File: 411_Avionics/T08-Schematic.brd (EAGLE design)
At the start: 63.1 x 25.4 mm, 42 parts, among them IC1 BQ24022, J1 USB-MICROB, J3 JST-PH-2-SMT-RA, U1 LP5907, U2 M25P10-AVMN6TP_TR, U3 LSM9DS0, U5 LTC1998, U6 ATMEGA32U4-AU, X1 8MHz

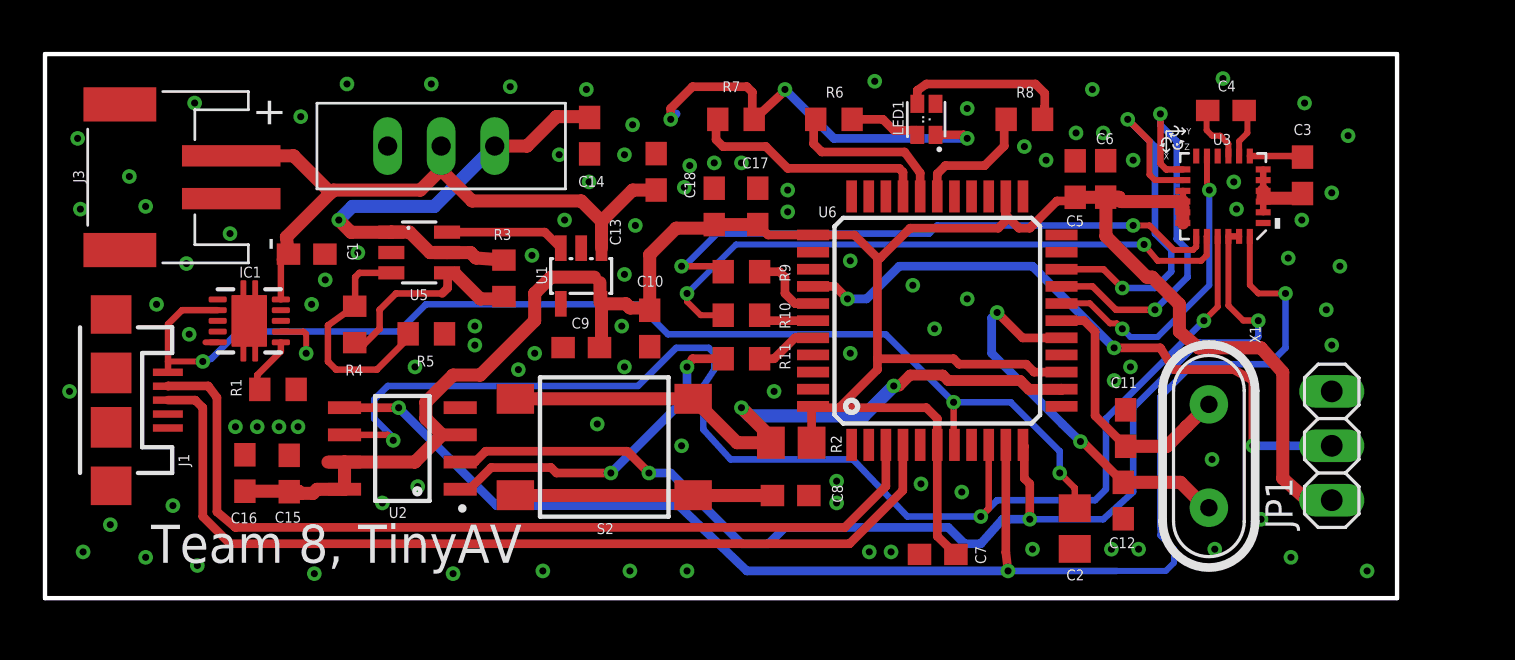
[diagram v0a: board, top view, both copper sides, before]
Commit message: Updated current limiting resistors to 0805 package.  Also fixed some oopsies on the layout (extra traces).
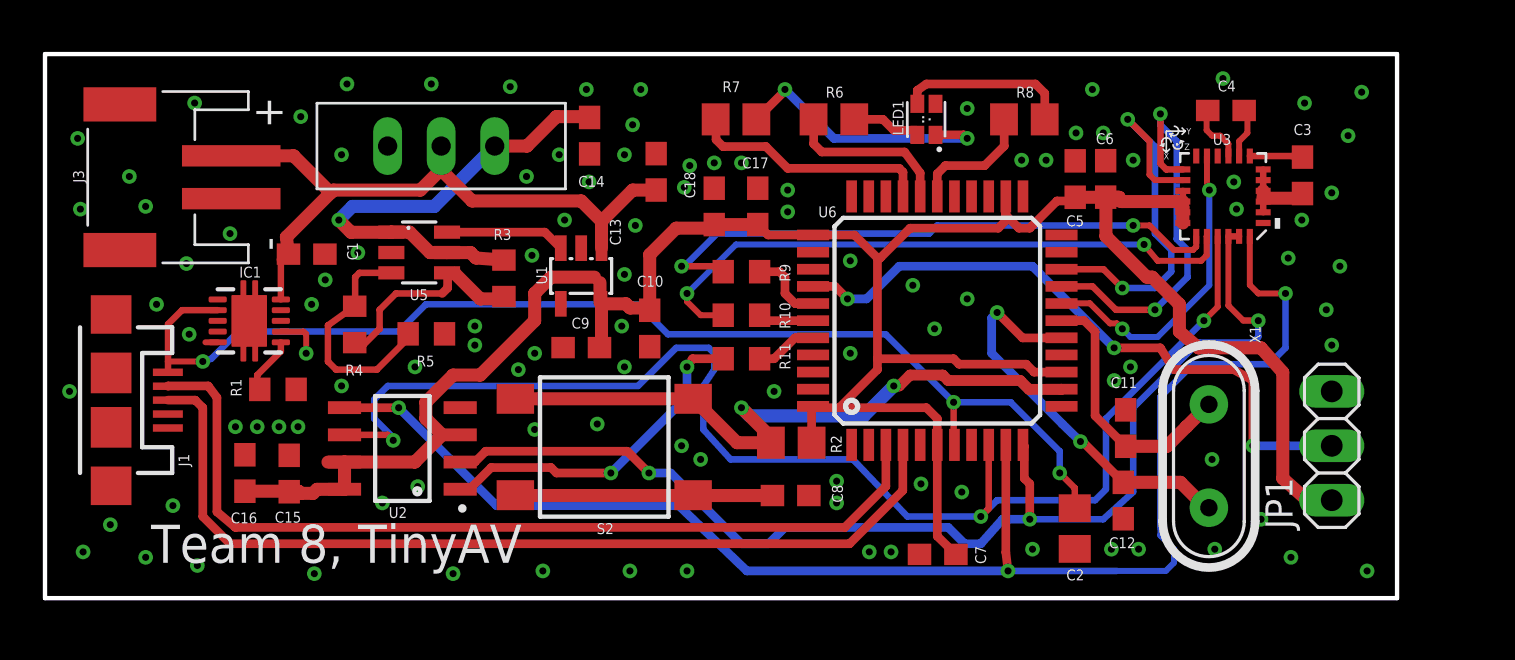
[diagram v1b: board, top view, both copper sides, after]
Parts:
- R6, R7, R8: device rcl:R0603 -> rcl:R0805
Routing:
- net N$1: track 19.5 -> 13.0 mm, vias 3 -> 2
- net GND: vias 99 -> 105
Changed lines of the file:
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@@
 <attribute name="NAME" x="18.183" y="11.322" size="0.508" layer="25" rot="R180"/>
 </element>
-<element name="R6" library="rcl" package="R0603" value="330" x="36.83" y="22.352" smashed="yes">
+<element name="R6" library="rcl" package="R0805" value="330" x="36.83" y="22.352" smashed="yes">
 <attribute name="NAME" x="36.449" y="23.368" size="0.508" layer="25"/>
 </element>
-<element name="R7" library="rcl" package="R0603" value="330" x="32.258" y="22.352" smashed="yes">
+<element name="R7" library="rcl" package="R0805" value="330" x="32.258" y="22.352" smashed="yes">
 <attribute name="NAME" x="31.623" y="23.622" size="0.508" layer="25"/>
 </element>
-<element name="R8" library="rcl" package="R0603" value="330" x="45.72" y="22.352" smashed="yes">
+<element name="R8" library="rcl" package="R0805" value="330" x="45.72" y="22.352" smashed="yes">
 <attribute name="NAME" x="45.339" y="23.368" size="0.508" layer="25"/>
 </element>
@@
 <via x="60.452" y="15.494" extent="1-16" drill="0.3302"/>
 <via x="58.801" y="23.114" extent="1-16" drill="0.3302"/>
-<via x="38.735" y="24.13" extent="1-16" drill="0.3302"/>
 <via x="31.242" y="20.32" extent="1-16" drill="0.3302"/>
 <via x="34.671" y="18.034" extent="1-16" drill="0.3302"/>
-<via x="45.72" y="21.082" extent="1-16" drill="0.3302"/>
+<via x="45.593" y="20.447" extent="1-16" drill="0.3302"/>
 <via x="48.895" y="23.749" extent="1-16" drill="0.3302"/>
 <via x="54.991" y="24.257" extent="1-16" drill="0.3302"/>
@@
 <via x="4.699" y="18.288" extent="1-16" drill="0.3302"/>
 <via x="1.778" y="2.159" extent="1-16" drill="0.3302"/>
+<via x="27.813" y="23.749" extent="1-16" drill="0.3302"/>
+<via x="22.86" y="7.874" extent="1-16" drill="0.3302"/>
+<via x="61.468" y="23.622" extent="1-16" drill="0.3302"/>
+<via x="30.607" y="6.477" extent="1-16" drill="0.3302"/>
+<via x="13.843" y="9.906" extent="1-16" drill="0.3302"/>
+<via x="13.843" y="20.701" extent="1-16" drill="0.3302"/>
+<via x="22.479" y="19.685" extent="1-16" drill="0.3302"/>
 </signal>
 <signal name="N$4">
@@
 <wire x1="40.056" y1="19.888" x2="39.878" y2="20.066" width="0.4064" layer="1"/>
 <wire x1="39.878" y1="20.066" x2="34.671" y2="20.066" width="0.4064" layer="1"/>
-<wire x1="31.242" y1="22.286" x2="31.408" y2="22.352" width="0.4064" layer="1"/>
+<wire x1="31.242" y1="22.286" x2="31.308" y2="22.352" width="0.4064" layer="1"/>
 <wire x1="34.671" y1="20.066" x2="33.655" y2="21.082" width="0.4064" layer="1"/>
 <wire x1="33.655" y1="21.082" x2="31.65" y2="21.082" width="0.4064" layer="1"/>
 <wire x1="31.65" y1="21.082" x2="31.327" y2="21.405" width="0.4064" layer="1"/>
 <wire x1="31.327" y1="21.405" x2="31.327" y2="22.333" width="0.4064" layer="1"/>
-<wire x1="31.327" y1="22.333" x2="31.408" y2="22.352" width="0.4064" layer="1"/>
+<wire x1="31.327" y1="22.333" x2="31.308" y2="22.352" width="0.4064" layer="1"/>
 </signal>
 <signal name="GREEN_LED">
@@
 <wire x1="40.856" y1="19.85" x2="40.132" y2="20.828" width="0.4064" layer="1"/>
 <wire x1="40.132" y1="20.828" x2="36.266" y2="20.828" width="0.4064" layer="1"/>
-<wire x1="35.873" y1="22.345" x2="35.98" y2="22.352" width="0.4064" layer="1"/>
+<wire x1="35.873" y1="22.345" x2="35.88" y2="22.352" width="0.4064" layer="1"/>
 <wire x1="36.266" y1="20.828" x2="35.883" y2="21.211" width="0.4064" layer="1"/>
 <wire x1="35.883" y1="21.211" x2="35.883" y2="22.349" width="0.4064" layer="1"/>
-<wire x1="35.883" y1="22.349" x2="35.98" y2="22.352" width="0.4064" layer="1"/>
+<wire x1="35.883" y1="22.349" x2="35.88" y2="22.352" width="0.4064" layer="1"/>
 </signal>
 <signal name="BLUE_LED">
@@
 <wire x1="43.867" y1="20.193" x2="44.78" y2="21.106" width="0.4064" layer="1"/>
 <wire x1="44.78" y1="21.106" x2="44.78" y2="22.342" width="0.4064" layer="1"/>
-<wire x1="44.78" y1="22.342" x2="44.87" y2="22.352" width="0.4064" layer="1"/>
+<wire x1="44.78" y1="22.342" x2="44.77" y2="22.352" width="0.4064" layer="1"/>
 </signal>
 <signal name="N$1">
 <contactref element="LED1" pad="1"/>
 <contactref element="R7" pad="2"/>
-<wire x1="29.464" y1="22.606" x2="29.21" y2="22.352" width="0.4064" layer="16"/>
-<via x="29.21" y="22.352" extent="1-16" drill="0.3302"/>
-<wire x1="29.21" y1="22.352" x2="29.21" y2="22.86" width="0.4064" layer="1"/>
-<wire x1="29.21" y1="22.86" x2="30.226" y2="23.876" width="0.4064" layer="1"/>
-<wire x1="30.226" y1="23.876" x2="32.766" y2="23.876" width="0.4064" layer="1"/>
-<wire x1="32.766" y1="23.876" x2="33.02" y2="23.622" width="0.4064" layer="1"/>
-<wire x1="33.02" y1="23.622" x2="33.02" y2="22.54" width="0.4064" layer="1"/>
-<wire x1="33.02" y1="22.54" x2="33.108" y2="22.352" width="0.4064" layer="1"/>
 <via x="43.053" y="21.463" extent="1-16" drill="0.3302"/>
 <via x="34.544" y="23.749" extent="1-16" drill="0.3302"/>
 <wire x1="34.544" y1="23.749" x2="34.544" y2="23.688" width="0.4064" layer="1"/>
-<wire x1="34.544" y1="23.688" x2="33.108" y2="22.352" width="0.4064" layer="1"/>
+<wire x1="34.544" y1="23.688" x2="33.208" y2="22.352" width="0.4064" layer="1"/>
 <wire x1="41.573" y1="21.627" x2="42.889" y2="21.627" width="0.4064" layer="1"/>
 <wire x1="42.889" y1="21.627" x2="43.053" y2="21.463" width="0.4064" layer="1"/>
@@
 <contactref element="LED1" pad="2"/>
 <contactref element="R6" pad="2"/>
-<wire x1="37.68" y1="22.352" x2="39.116" y2="22.352" width="0.4064" layer="1"/>
+<wire x1="37.78" y1="22.352" x2="39.116" y2="22.352" width="0.4064" layer="1"/>
 <wire x1="39.116" y1="22.352" x2="39.624" y2="21.844" width="0.4064" layer="1"/>
 <wire x1="39.624" y1="21.844" x2="40.686" y2="21.844" width="0.4064" layer="1"/>
@@
 <contactref element="LED1" pad="3"/>
 <contactref element="R8" pad="2"/>
-<wire x1="46.57" y1="22.352" x2="46.67" y2="22.926" width="0.4064" layer="1"/>
+<wire x1="46.67" y1="22.352" x2="46.67" y2="22.926" width="0.4064" layer="1"/>
 <wire x1="40.723" y1="23.077" x2="40.723" y2="23.705" width="0.4064" layer="1"/>
 <wire x1="40.723" y1="23.705" x2="41.148" y2="24.003" width="0.4064" layer="1"/>

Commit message: Added resistors to D+/D-, removed incorrect reset button cap, fixed RGB LED VCC
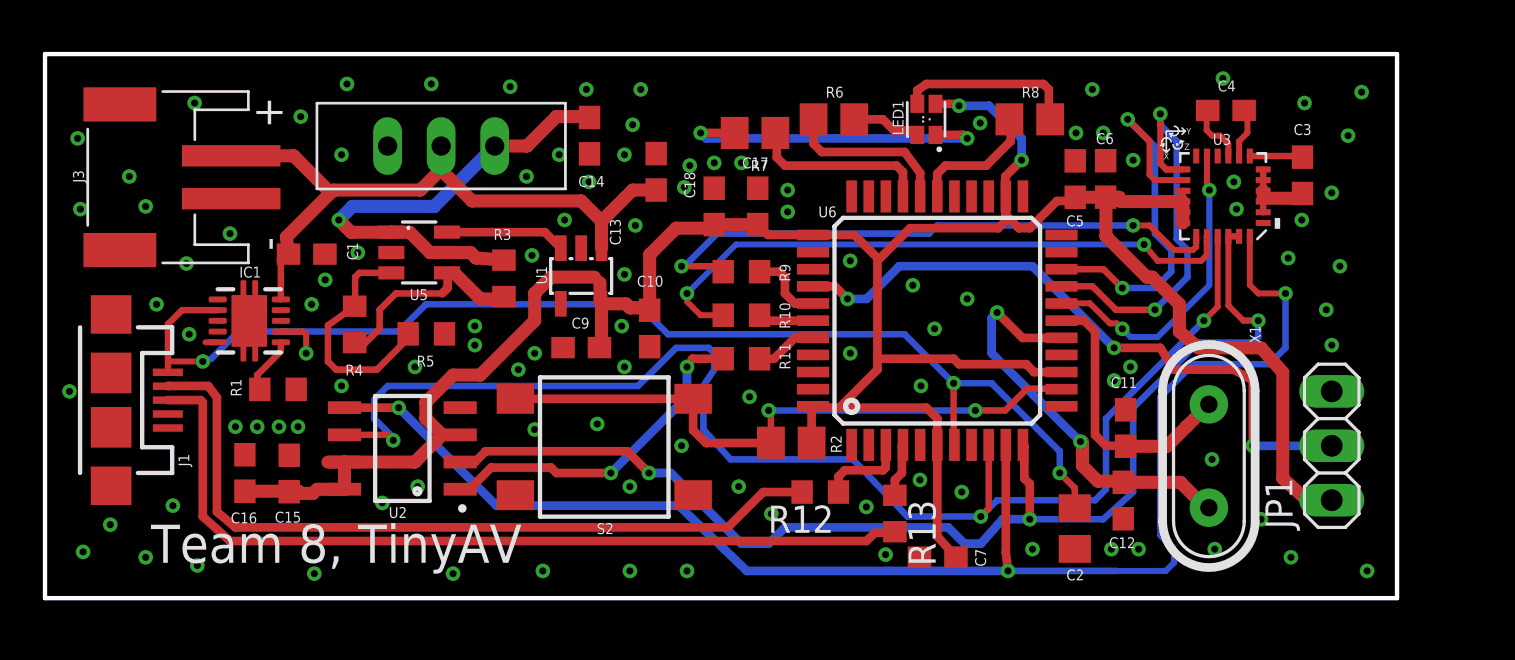
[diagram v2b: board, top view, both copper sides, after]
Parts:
- removed C8: 10u, rcl:C0603
- added R12, R13: 22, rcl:R0603
- moved R7 1.09 mm to (33.1, 21.7), turned to 180 degrees
- moved R8 0.25 mm to (46.0, 22.4)
- moved C7 0.13 mm to (41.7, 1.92)
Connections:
- new net N$47: R13.1, U6.4
- net D+: now also R13.2; no longer U6.4
- net D-: now also R12.2; no longer U6.3
- net GND: now also S2.1, S2.2; no longer C8.2, LED1.4
- net N$6: now also R12.1, U6.3; no longer C8.1, S2.1, S2.2
- net VCC: now also LED1.4
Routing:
- net N$6: track 12.0 -> 4.16 mm
- net VCC: track 121.3 -> 129.1 mm, vias 0 -> 2
- net D-: track 42.1 -> 36.2 mm
- net D+: track 43.2 -> 39.9 mm
- net RED_LED: track 11.5 -> 8.48 mm
- net N$1: track 13.0 -> 15.7 mm
- net N$47: track 0.00 -> 2.51 mm
- net N$3: track 31.2 -> 29.3 mm
- net VBUS1: track 55.3 -> 56.2 mm
- net N$5: track 18.6 -> 19.3 mm
- net N$2: track 12.4 -> 12.9 mm
- net GND: vias 105 -> 104
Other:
- board text added: "Avoid 45s"

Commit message: Lots of changes to layout!
-Added 6 pin header
-Added status LEDs
-Added Power LEDs`
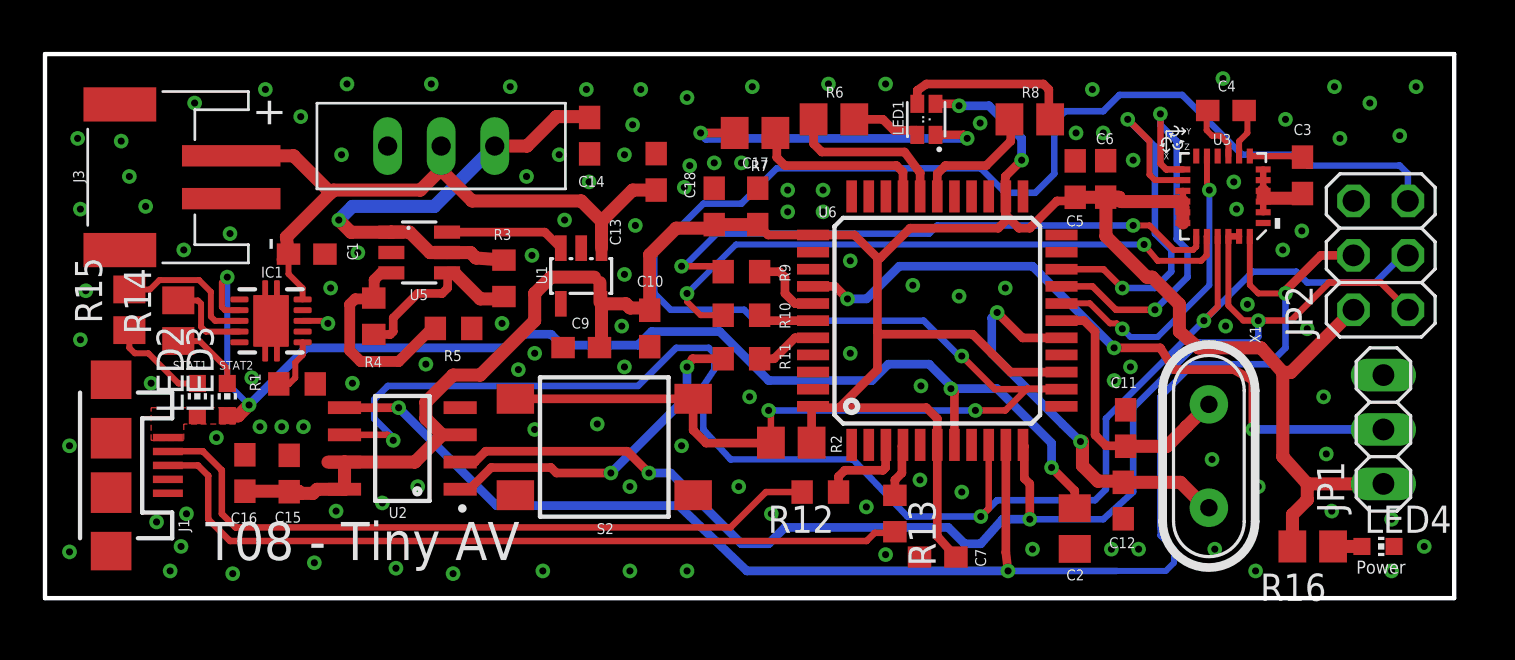
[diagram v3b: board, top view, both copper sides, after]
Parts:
- added JP2: (no value), pinhead:2X03
- added LED2, LED3, LED4: (no value), adafruit:CHIP-LED0603
- added R14, R15, R16: 330, rcl:R0805
- moved J1 3.05 mm to (3.09, 6.20)
- moved JP1 2.53 mm to (62.5, 7.87)
- moved R5 1.30 mm to (19.1, 12.6)
- moved IC1 1.02 mm to (10.6, 12.9)
- moved R4 0.97 mm to (15.3, 13.2)
- moved R1 0.92 mm to (11.8, 10.0)
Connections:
- new net N$48: LED2.C, R15.1
- new net N$49: LED3.C, R14.1
- new net N$50: IC1.3, R15.2
- new net N$51: IC1.4, R14.2
- new net N$53: LED4.A, R16.1
- net CLK: now also JP2.3
- net GND: now also JP2.6, LED4.C
- net MISO: now also JP2.1
- net MOSI: now also JP2.4
- net N$3: now also JP2.5
- net VBUS1: now also LED2.A, LED3.A
- net VCC: now also JP2.2, R16.2
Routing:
- net N$3: track 29.3 -> 95.5 mm, vias 2 -> 3
- net CLK: track 63.9 -> 75.1 mm
- net VCC: track 129.1 -> 138.9 mm
- net MISO: track 56.0 -> 64.2 mm
- net N$50: track 0.00 -> 6.79 mm
- net N$48: track 0.00 -> 4.69 mm
- net N$51: track 0.00 -> 4.10 mm
- net MOSI: track 69.3 -> 73.3 mm
- net N$49: track 0.00 -> 3.51 mm
- net D-: track 36.2 -> 33.0 mm
- net D+: track 39.9 -> 36.8 mm
- net VBUS1: track 56.2 -> 58.4 mm, vias 3 -> 4
- net FIRE_EN: track 30.4 -> 32.1 mm
- net GND: track 6.99 -> 5.53 mm, vias 104 -> 122
- net N$12: track 10.1 -> 8.67 mm
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- added copper zone on layer 1, net VBUS1
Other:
- board size 63.1 x 25.4 mm -> 65.8 x 25.4 mm
- board text added: "Power"
- board text added: "STAT1"
- board text added: "STAT2"
- board text added: "T08 - Tiny AV"
- board text removed: "Team 8, TinyAV"

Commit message: Added 0 ohm resistor to #HWB line. Added test points to unpopulated GPIO.
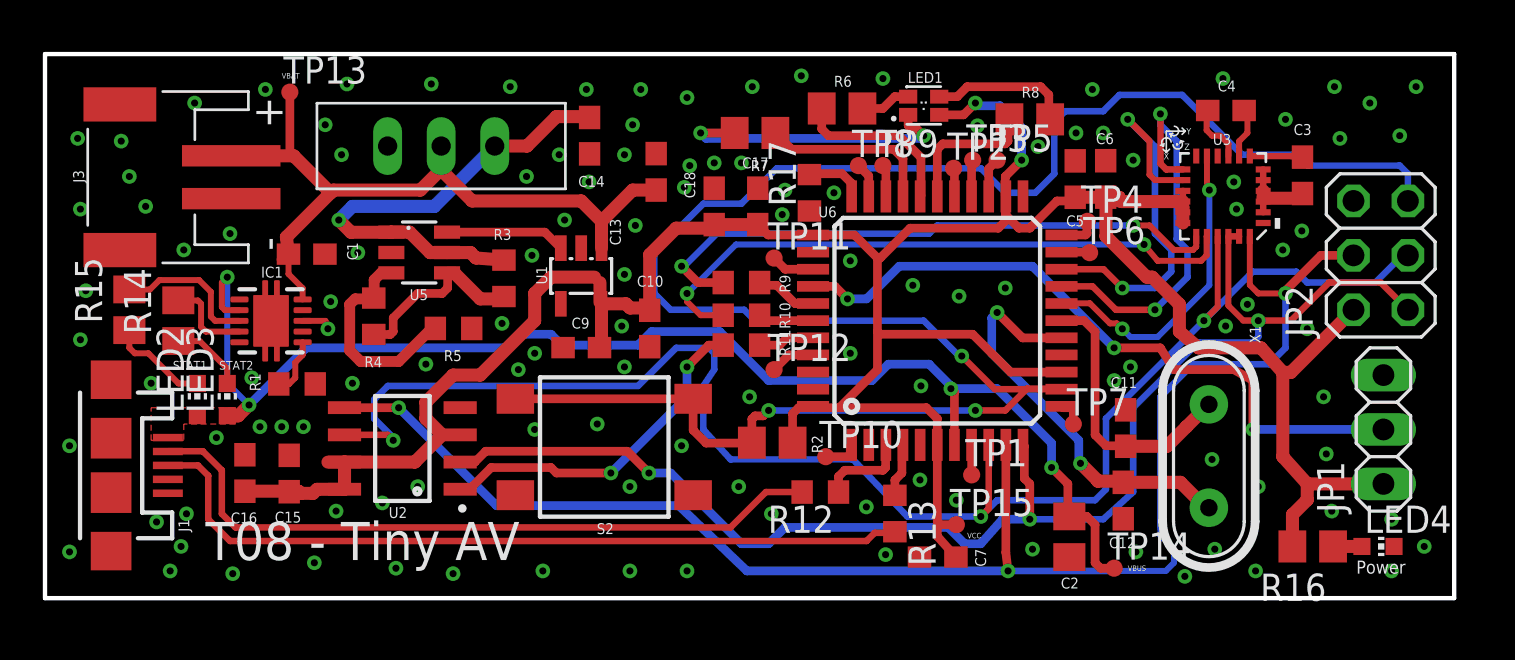
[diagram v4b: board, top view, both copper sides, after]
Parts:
- added R17: 0, rcl:R0603
- added TP1, TP10, TP11, TP12, TP13, TP14, TP15, TP2, TP3, TP4, TP5, TP6, TP7, TP8, TP9: TPTP08R, testpad:TP08R
- moved R2 0.89 mm to (33.9, 7.26)
- moved LED1 0.65 mm to (41.0, 23.0), turned to 90 degrees
- moved R11 0.63 mm to (32.5, 11.8)
- moved R6 0.63 mm to (37.2, 22.9)
- moved R9 0.51 mm to (32.5, 14.7)
- moved C2 0.46 mm to (47.8, 2.87)
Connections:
- new net N$52: TP3.TP, U6.26
- new net N$54: TP12.TP, U6.41
- new net N$55: TP11.TP, U6.36
- new net N$56: TP10.TP, U6.1
- new net N$57: TP9.TP, U6.31
- new net N$58: TP8.TP, U6.32
- new net N$59: TP7.TP, U6.12
- new net N$60: TP1.TP, U6.8
- new net N$61: TP2.TP, U6.27
- new net N$62: TP4.TP, U6.22
- new net N$63: TP5.TP, U6.25
- new net N$64: TP6.TP, U6.21
- new net N$65: R17.2, U6.33
- net GND: now also R17.1; no longer U6.33
- net N$13: now also TP13.TP
- net VBUS1: now also TP14.TP
- net VCC: now also TP15.TP
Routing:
- net VBUS1: track 58.4 -> 62.8 mm
- net N$13: track 32.6 -> 35.7 mm
- net N$65: track 0.00 -> 2.78 mm
- net VCC: track 138.9 -> 141.1 mm
- net N$1: track 15.7 -> 13.6 mm
- net N$54: track 0.00 -> 2.10 mm
- net N$55: track 0.00 -> 2.04 mm
- net N$63: track 0.00 -> 1.86 mm
- net N$62: track 0.00 -> 1.79 mm
- net N$8: track 8.39 -> 6.64 mm
- net N$56: track 0.00 -> 1.72 mm
- net N$52: track 0.00 -> 1.71 mm
- net N$58: track 0.00 -> 1.64 mm
- net N$57: track 0.00 -> 1.50 mm
- net N$60: track 0.00 -> 1.40 mm
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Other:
- board text added: "VBAT"
- board text added: "VBUS"
- board text added: "VCC"
